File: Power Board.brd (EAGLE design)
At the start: 64.8 x 91.4 mm, 36 parts, among them Q1 IRLB8743PBF, U1 S18V20F12, U2 D24V22F3, U3 D24V22F5, U4 LTC7004, U5 CD4011BPWR

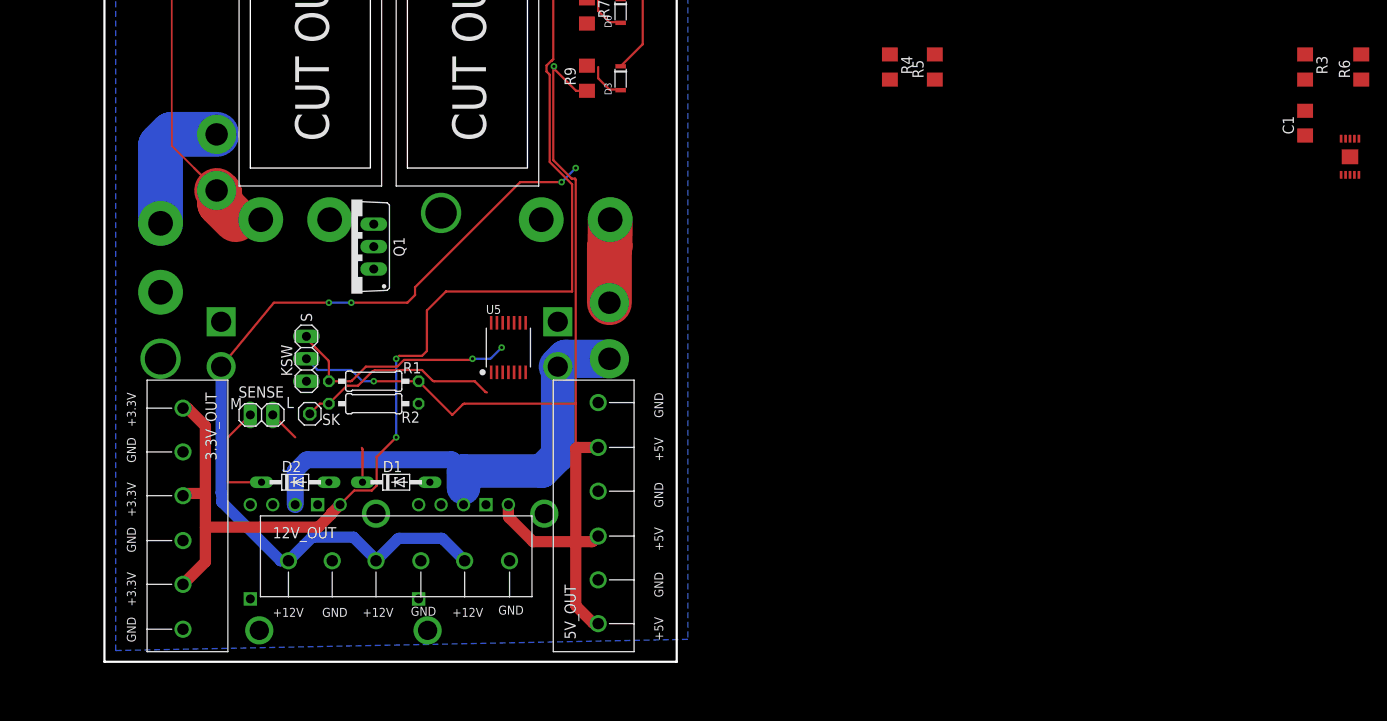
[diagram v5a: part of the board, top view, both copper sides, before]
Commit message: Add Simple Switcher 5V regulator design (still needs to be CADed)
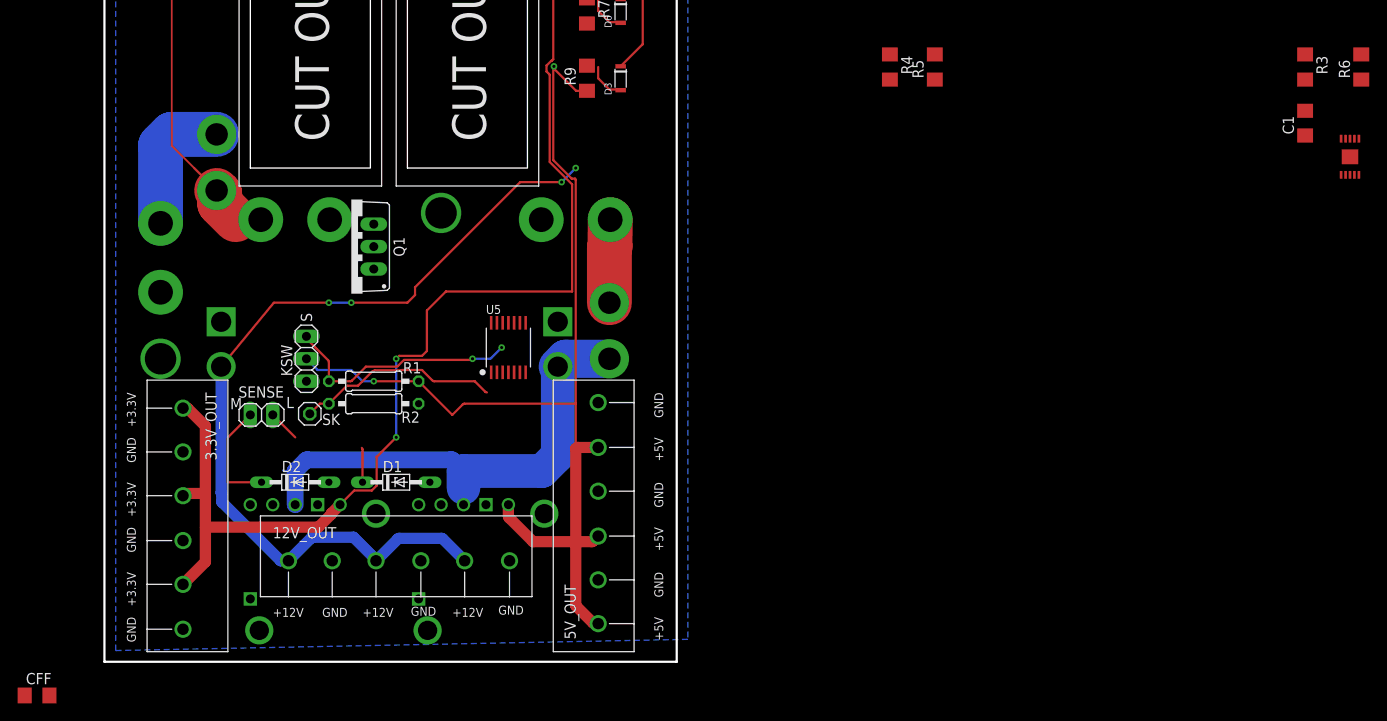
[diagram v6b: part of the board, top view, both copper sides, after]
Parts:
- added CFF: 100 pF, rcl:C1206

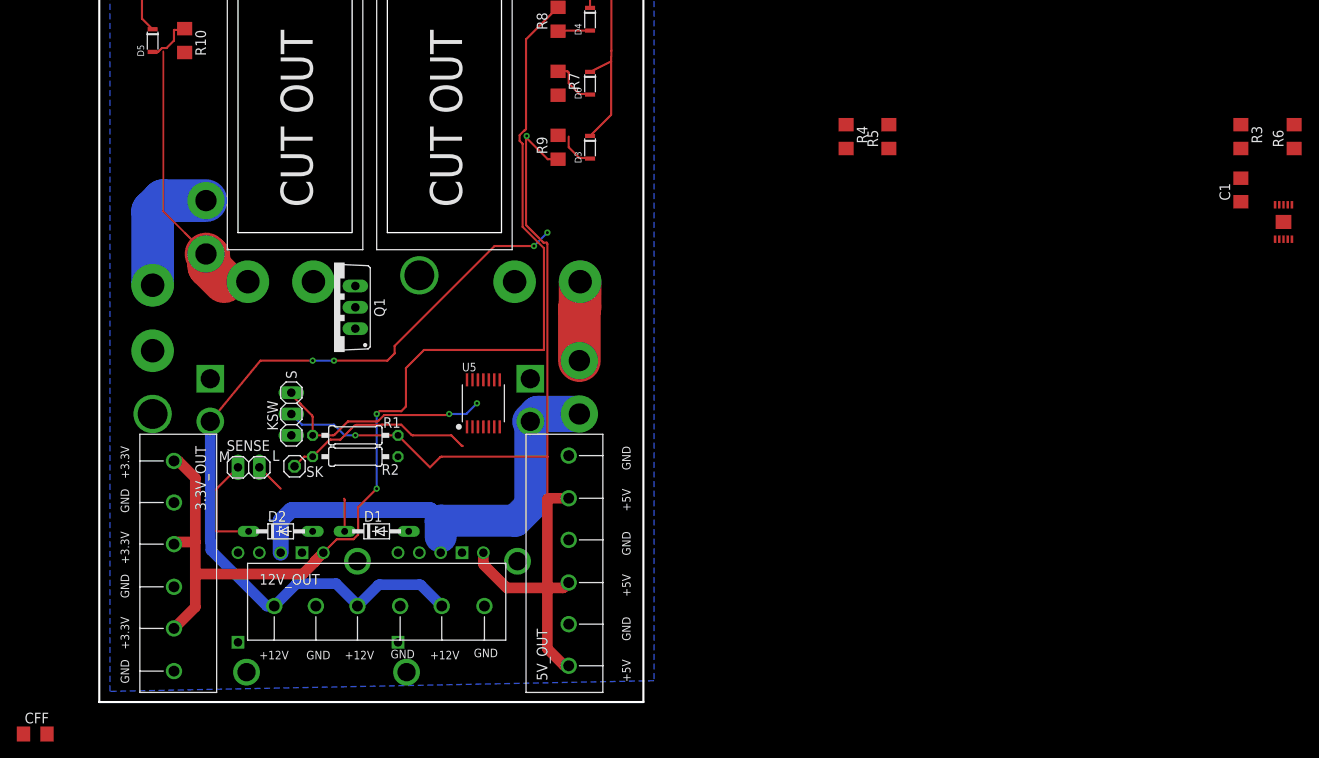
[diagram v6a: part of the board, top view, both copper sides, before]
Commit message: Reroute top of board for new surface-mount parts
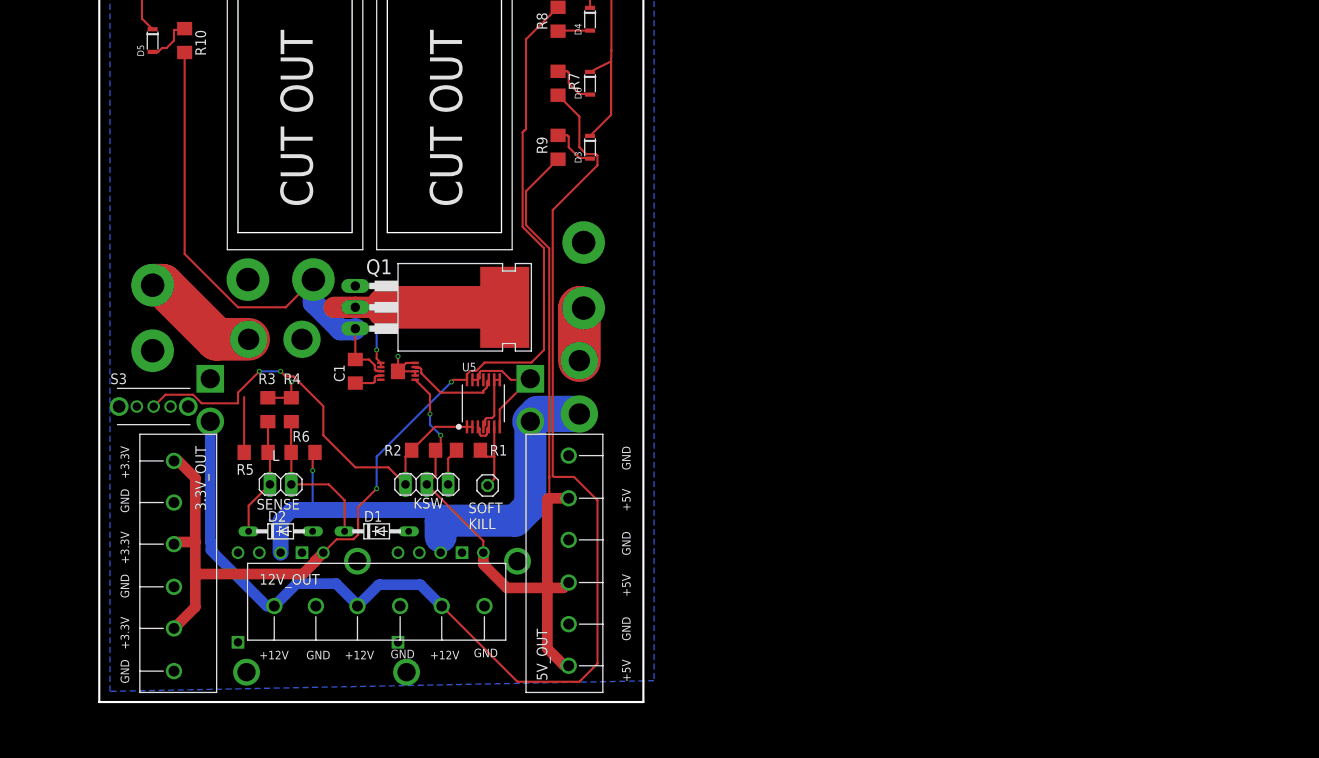
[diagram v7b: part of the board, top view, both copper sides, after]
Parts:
- removed CFF: 100 pF, rcl:C1206
- added S3: OS102011MS2QN1, Power Board Custom:OS102011MS2Q
- Q1: device transistor-power:TO220BV -> Power Board Custom:TO220
- R1, R2: device resistor:0207/10 -> rcl:R1206
- R3, R4: value 3.3K -> 3.3K 0.1%
- R5: value 3.3K -> 22K 0.1%
- R6: value 22K -> 22K 0.1%
- moved R6 123.8 mm to (7.75, 56.4), turned to 0 degrees
- moved R3 120.3 mm to (3.56, 61.5)
- moved C1 107.6 mm to (14.0, 66.0)
- moved U4 106.9 mm to (19.1, 66.0), turned to 90 degrees
- moved R5 84.2 mm to (2.16, 56.4), turned to 180 degrees
- moved R4 73.6 mm to (6.35, 61.5)
- moved SKSW 23.1 mm to (29.7, 52.5)
- moved KSW 18.2 mm to (22.5, 52.6), turned to 0 degrees
- moved S1 14.2 mm to (3.81, 71.1), turned to 90 degrees
- moved R1 13.6 mm to (27.4, 56.6)
- moved Q1 8.89 mm to (20.3, 73.7), turned to 270 degrees
- moved R2 8.16 mm to (22.1, 56.6), turned to 0 degrees
- moved LOGIC_BATT 4.38 mm to (41.1, 77.5), turned to 90 degrees
- moved SENSE 4.32 mm to (5.08, 52.6)
- moved MOTOR_PWR 0.25 mm to (5.08, 77.0), turned to 0 degrees
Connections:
- net N$8 renamed KFET_G
- net N$9 renamed M_PWR
- net GND: now also R1.1, S3.L; no longer R2.1
- net KILL_SIG: now also R2.1, S3.C; no longer R1.1
- net MOTOR_V+: now also Q1.D@1, Q1.D@2; no longer Q1.D
- net SOFT_KILL: now also R1.2; no longer R2.2
- net VCC: now also R2.2; no longer R1.2
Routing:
- net M_PWR: track 0.00 -> 62.4 mm
- net +12V: track 100.3 -> 149.2 mm, vias 4 -> 0
- net GND: track 34.4 -> 65.8 mm
- net KILL_SIG: track 27.2 -> 53.7 mm
- net VCC: track 119.7 -> 105.1 mm
- net SOFT_KILL: track 23.1 -> 9.28 mm
- net KFET_G: track 0.00 -> 12.4 mm, vias 0 -> 1
- net N$4: track 0.00 -> 11.5 mm
- net LOG_VSENS: track 7.49 -> 18.3 mm
- net N$3: track 0.00 -> 7.18 mm
- net LOG_VIN: track 58.6 -> 65.6 mm, vias 0 -> 1
- net +3V3: track 131.3 -> 125.7 mm
- net N$11: track 0.00 -> 3.70 mm
- net MOTOR_V+: track 30.4 -> 26.9 mm
- net N$2: track 0.00 -> 2.96 mm
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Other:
- board text added: "SOFT KILL"
- board text removed: "M"
- board text removed: "S"
- board text removed: "SK"

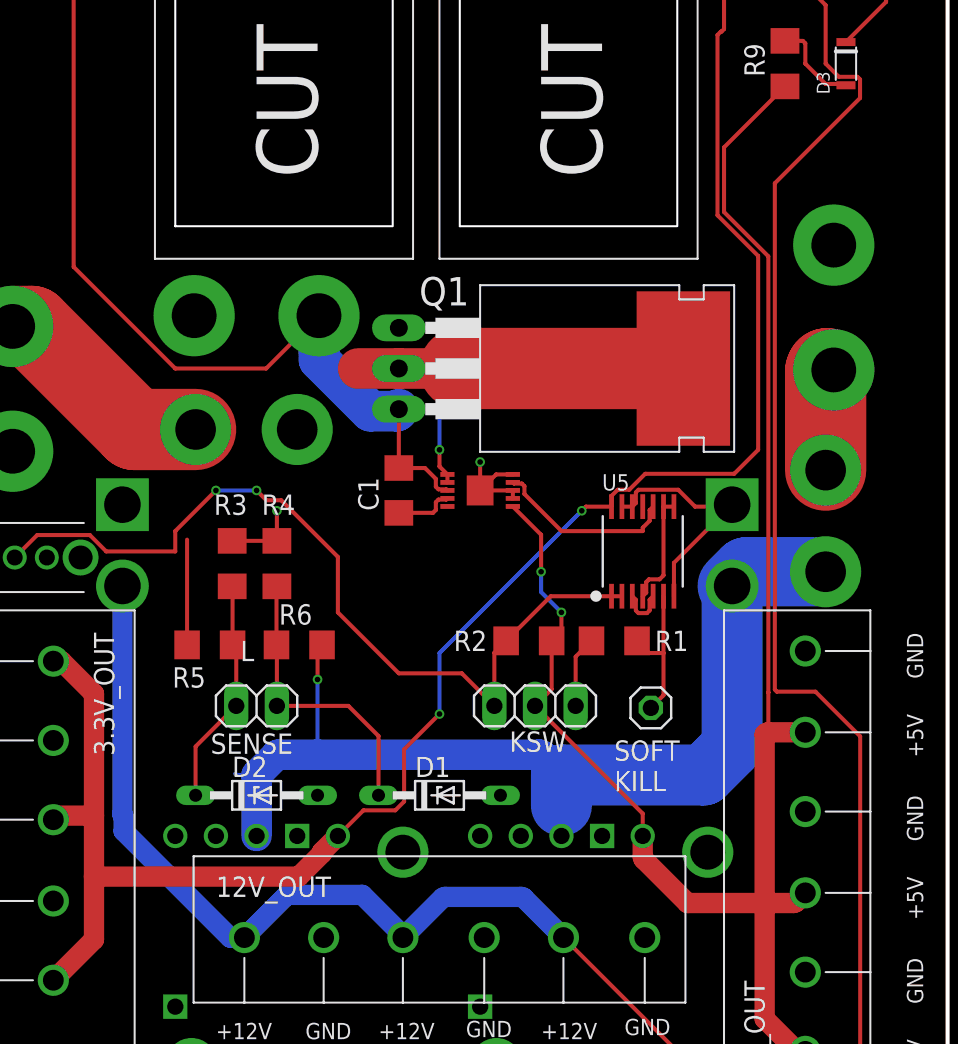
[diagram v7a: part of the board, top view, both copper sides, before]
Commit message: Done with Simple Switcher-based voltage regulator
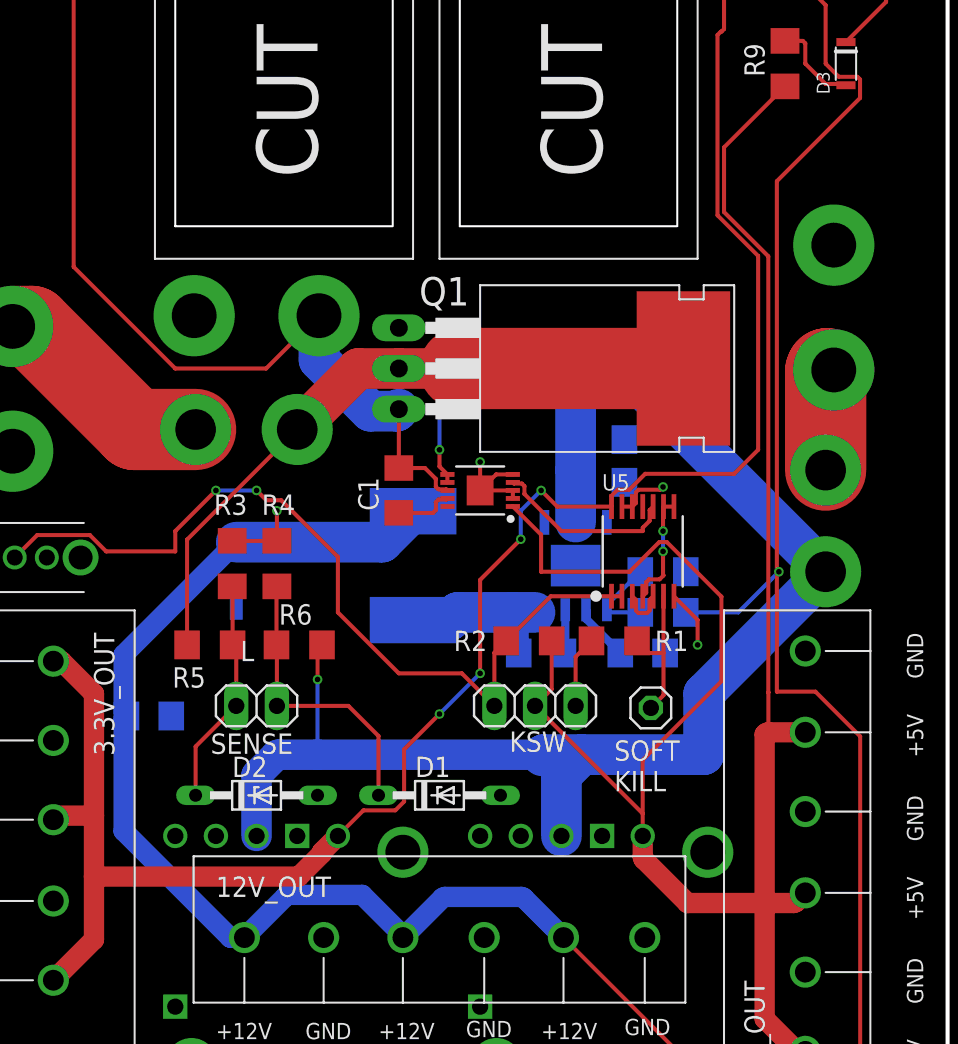
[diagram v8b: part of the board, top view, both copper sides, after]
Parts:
- removed U1: S18V20F12, Power Board Custom:S18V20
- added C2, C5, C7: 1uF, rcl:C1206
- added C3: 10uF, rcl:C1206
- added C4: .22uF, rcl:C1206
- added C6: 16SVPF82M, Power Board Custom:16SVPF82M
- added L1: SRR1280-180M, Power Board Custom:SRR1280
- added R12: 100k, rcl:R1206
- added R13: 9.09k, rcl:R1206
- added U6: LMR33630ADDA, Power Board Custom:HSOIC-8-POWERPAD
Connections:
- new net 12VREG_SW: C5.1, L1.1, U6.8
- new net 12V_BOOT: C5.2, U6.7
- new net 12V_FB: R12.2, R13.1, U6.5
- new net N$8: C2.1, U6.6
- net +12V: now also C6.POS, C7.1, L1.2, R12.1; no longer U1.VOUT
- net GND: now also C2.2, C3.2, C4.2, C6.NEG, C7.2, R13.2, U6.1, U6.THERMAL; no longer U1.GND1, U1.GND2
- net LOG_VIN: now also C3.1, C4.1, U6.2, U6.3; no longer U1.VIN
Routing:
- net LOG_VIN: track 65.6 -> 95.6 mm
- net +12V: track 149.2 -> 173.7 mm, vias 0 -> 1
- net VCC: track 105.1 -> 129.0 mm, vias 2 -> 0
- net MOTOR_V+: track 26.9 -> 42.0 mm
- net 12VREG_SW: track 0.00 -> 11.2 mm
- net GND: track 65.8 -> 57.4 mm, vias 4 -> 6
- net 12V_FB: track 0.00 -> 5.36 mm
- net N$8: track 0.00 -> 3.65 mm
- net +3V3: track 125.7 -> 128.8 mm, vias 2 -> 4
- net 12V_BOOT: track 0.00 -> 2.81 mm
- net M_PWR: track 62.4 -> 60.0 mm
- net N$3: track 7.18 -> 7.21 mm, vias 0 -> 2
